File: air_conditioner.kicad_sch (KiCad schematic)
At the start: 6 parts, among them J18 Conn_01x90_3Row_Socket, K2 1500A, K3 1502, K4 1500B, M2 Fan1, M3 Fan2

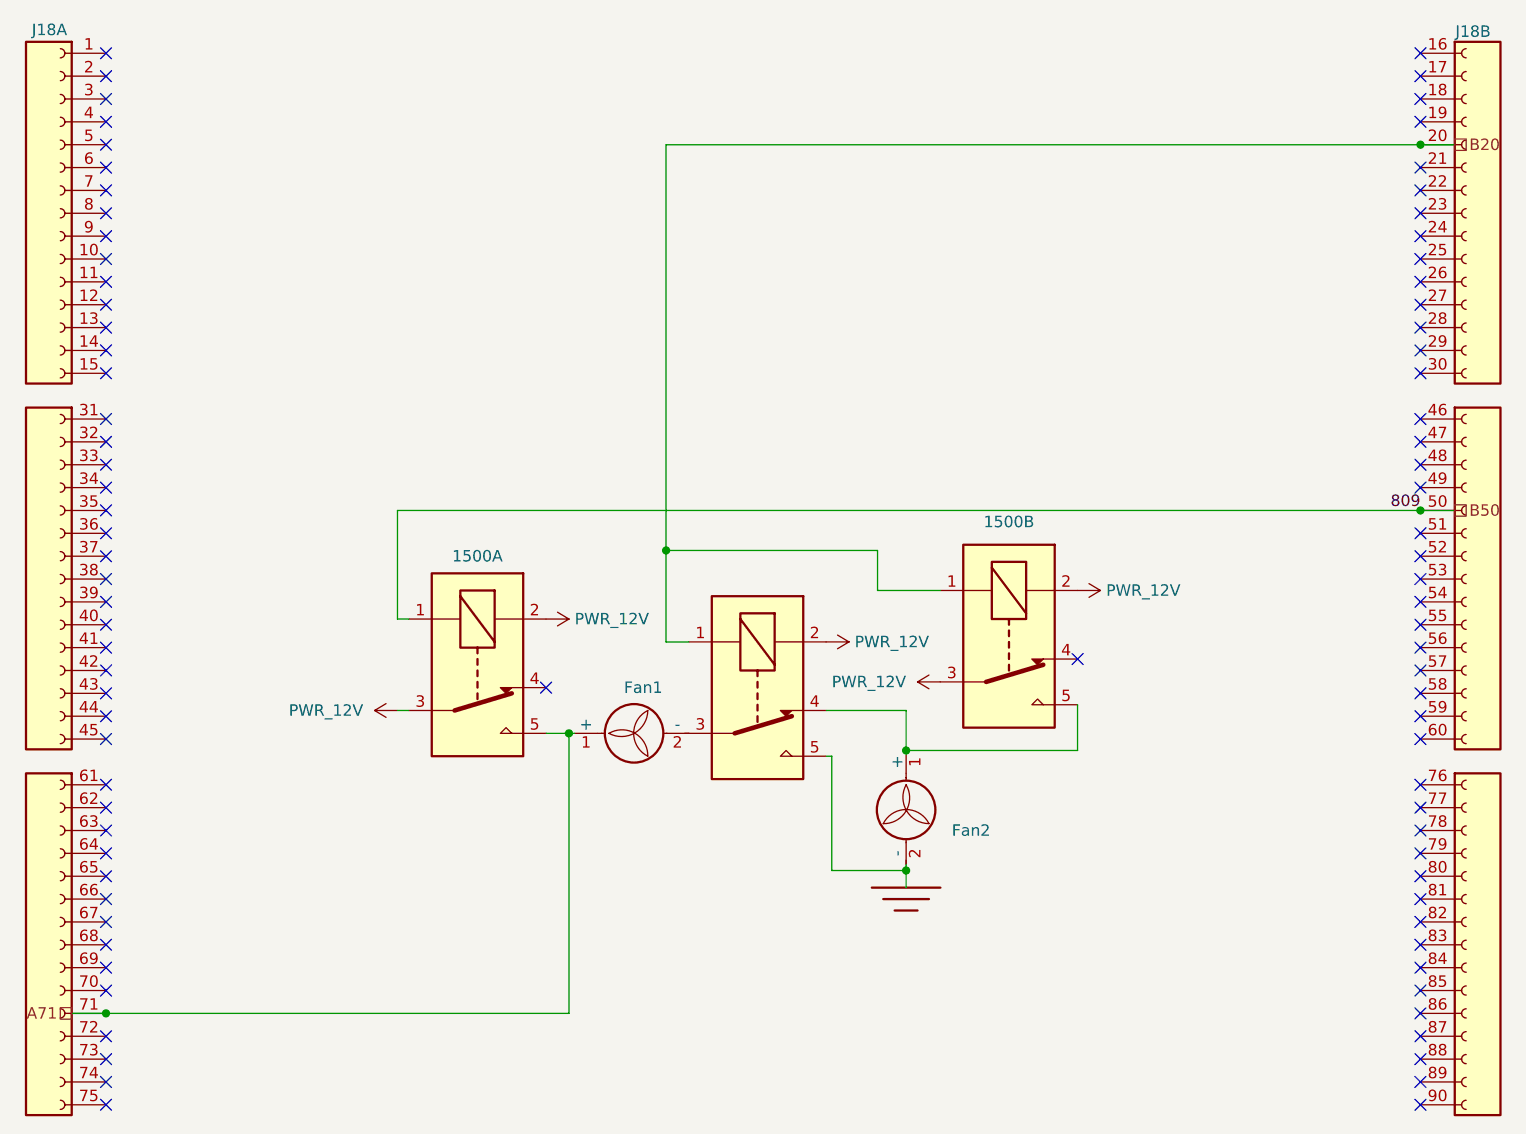
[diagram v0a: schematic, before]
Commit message: air conditioner updated
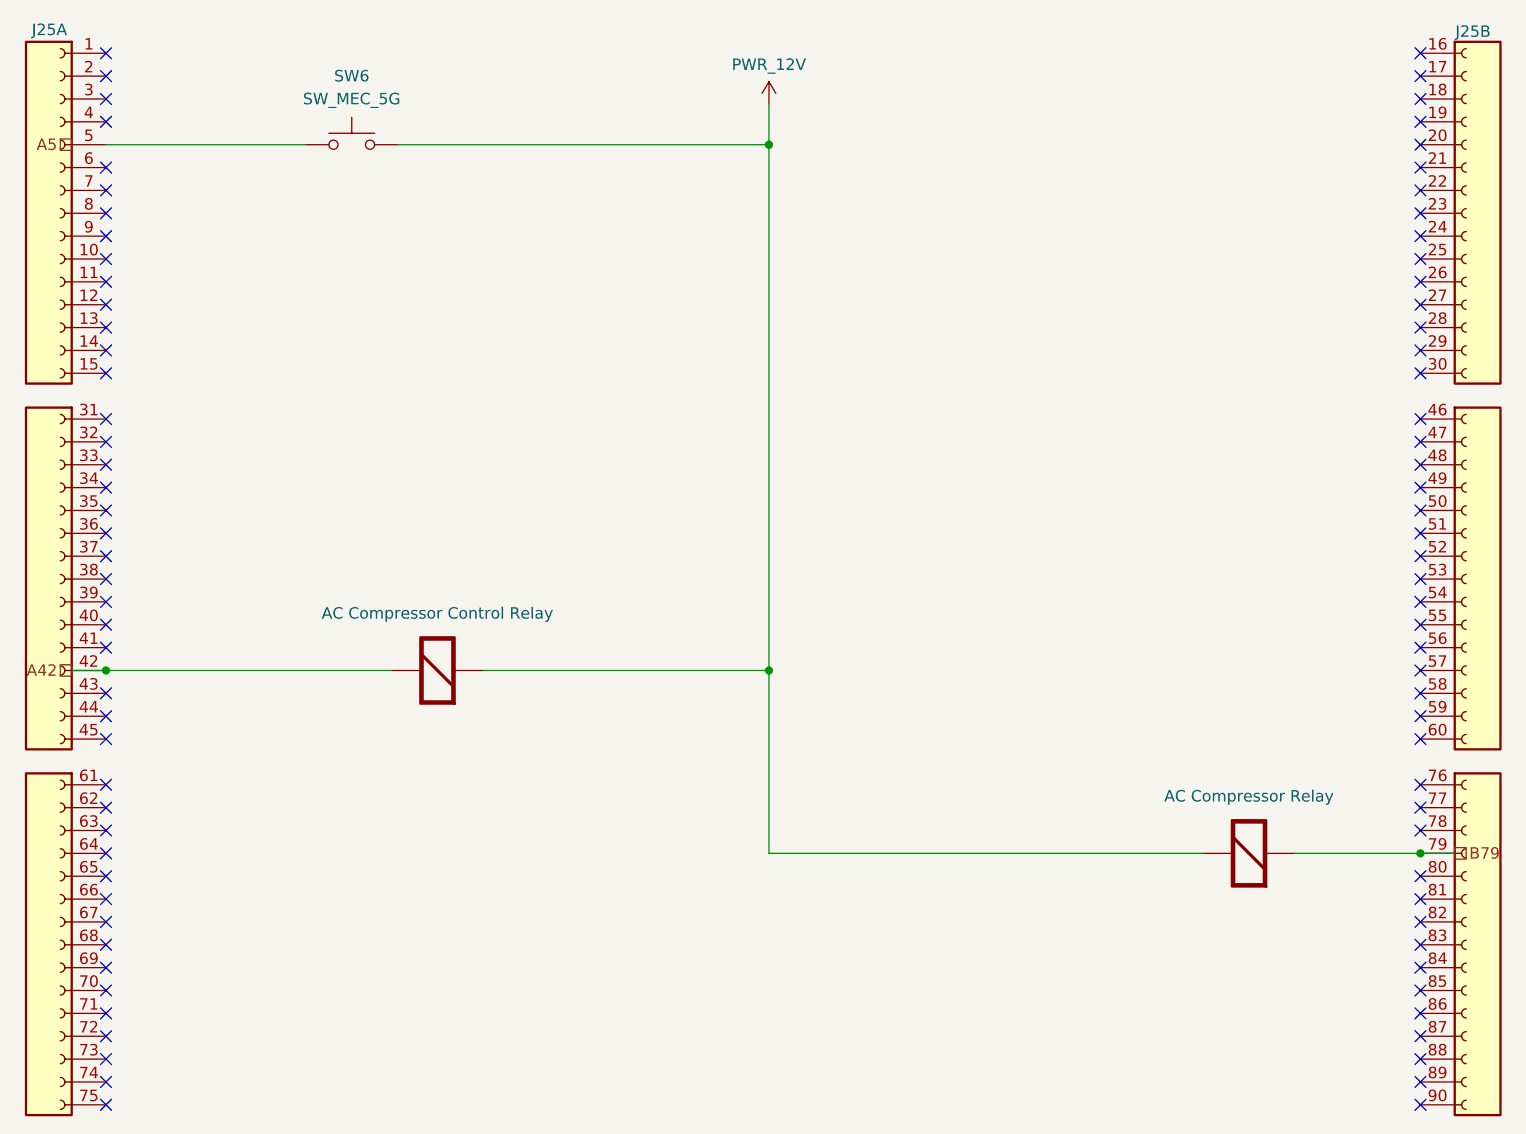
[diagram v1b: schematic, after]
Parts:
- removed K2: 1500A, PCM_SparkFun-Electromechanical:Relay_SPDT_20A_27.6x32.0mm, symbol SparkFun-Electromechanical:Relay_SPDT_20A_5V_27.6x32.0mm
- removed K3: 1502, PCM_SparkFun-Electromechanical:Relay_SPDT_20A_27.6x32.0mm, symbol SparkFun-Electromechanical:Relay_SPDT_20A_5V_27.6x32.0mm
- removed K4: 1500B, PCM_SparkFun-Electromechanical:Relay_SPDT_20A_27.6x32.0mm, symbol SparkFun-Electromechanical:Relay_SPDT_20A_5V_27.6x32.0mm
- removed M2: Fan1, symbol Motor:Fan
- removed M3: Fan2, symbol Motor:Fan
- added Re13: AC Compressor Control Relay, symbol Elektuur_1:Re
- added Re14: AC Compressor Relay, symbol Elektuur_1:Re
- added SW6: SW_MEC_5G, symbol Switch:SW_MEC_5G
- renumbered J18 to J25
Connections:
- net PWR_12V: now also Re13.2 (-), Re14.1 (+), SW6.3 (B), SW6.4 (B)
- net B79: now reaches J25.79 (B79)
- net B79: now also Re14.2 (-)
- net A42: now reaches J25.42 (A42)
- net A42: now also Re13.1 (+)
- net at J25.5 (A5): now also SW6.1 (A), SW6.2 (A)
- net A71: no longer names the net of J25.71 (A71)
- net B20: no longer names the net of J25.20 (B20)
- net B50: no longer names the net of J25.50 (B50)
- no-connect marks 89 -> 87
